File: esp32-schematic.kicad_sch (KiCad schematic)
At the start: 1 part, among them U1 ESP32-S3-DEVKITC-1U-N8R2

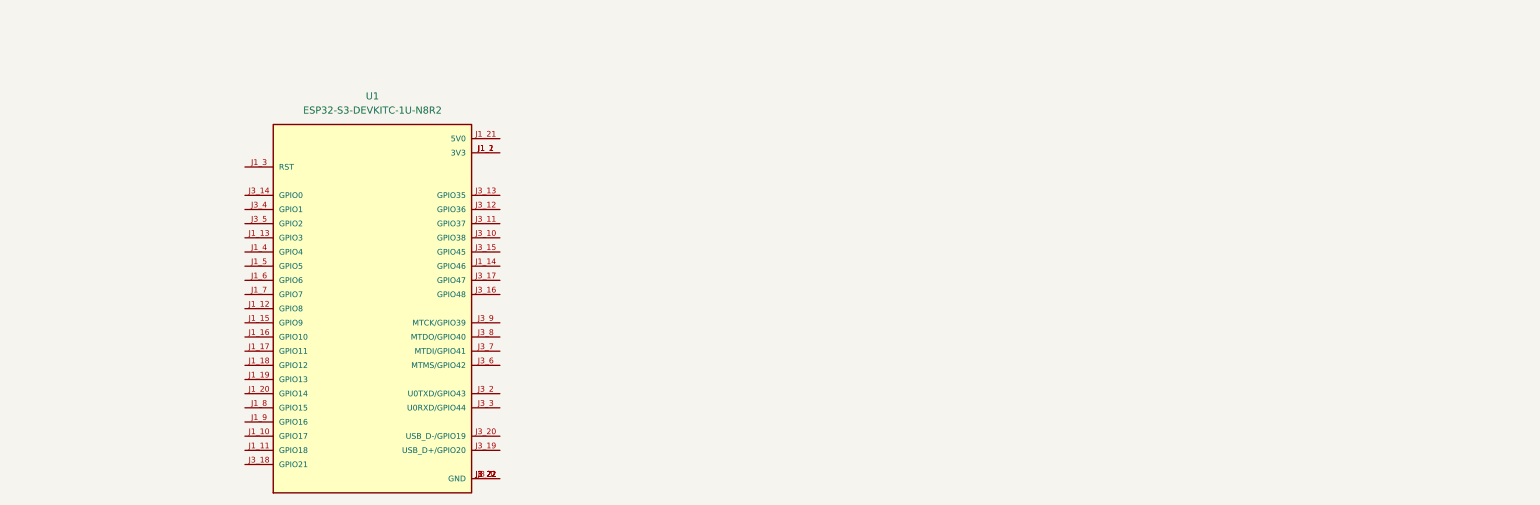
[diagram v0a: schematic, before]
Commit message: GPS added and CAN in progress
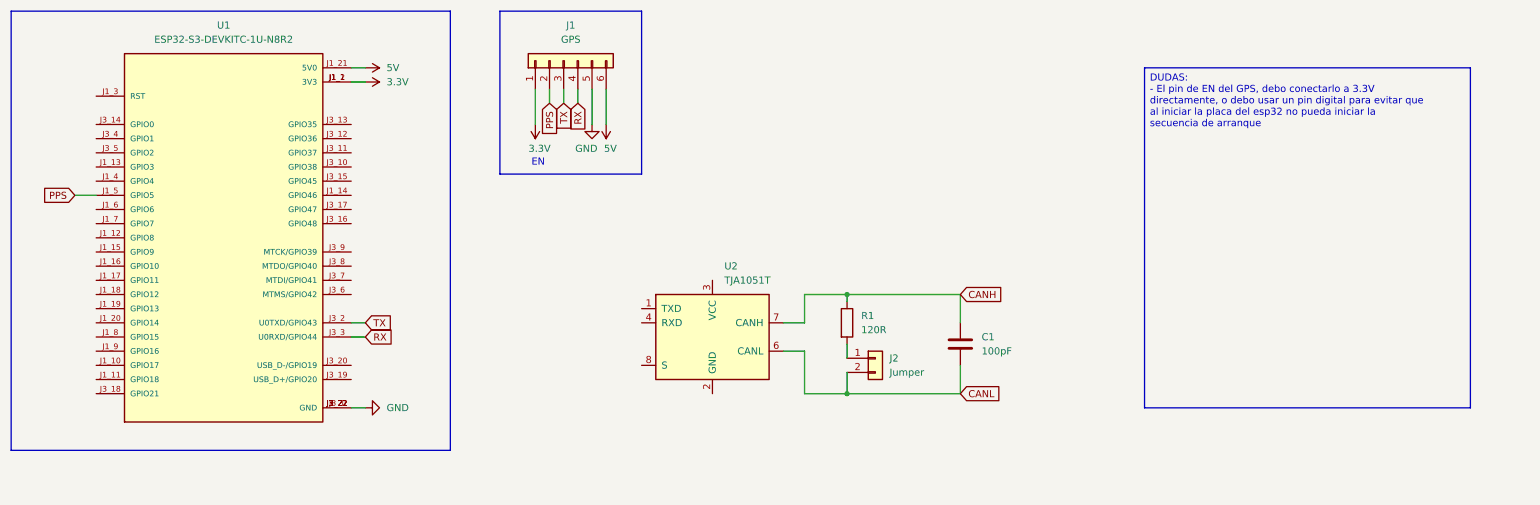
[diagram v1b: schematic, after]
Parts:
- added C1: 100pF, Capacitor_SMD:C_0805_2012Metric, symbol Device:C
- added J1: GPS, Conn_01x06:PinHeader_1x06_P2.54mm_Vertical, symbol Connector_Generic:Conn_01x06
- added J2: Jumper, Connector_PinHeader_1.00mm:PinHeader_1x02_P1.00mm_Vertical, symbol Connector_Generic:Conn_01x02
- added R1: 120R, Resistor_SMD:R_1206_3216Metric, symbol Device:R
- added U2: TJA1051T, Package_SO:SOIC-8_3.9x4.9mm_P1.27mm, symbol Interface_CAN_LIN:TJA1051T
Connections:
- net 3.3V: now reaches U1.J1_1 (3V3), U1.J1_2 (3V3)
- net 3.3V: now also J1.1 (Pin_1)
- net 5V: now reaches U1.J1_21 (5V0)
- net 5V: now also J1.6 (Pin_6)
- net GND: now reaches U1.J1_22 (GND), U1.J3_1 (GND), U1.J3_21 (GND), U1.J3_22 (GND)
- net GND: now also J1.5 (Pin_5)
- net PPS: now reaches U1.J1_5 (GPIO5)
- net PPS: now also J1.2 (Pin_2)
- net TX: now reaches U1.J3_2 (U0TXD/GPIO43)
- net TX: now also J1.3 (Pin_3)
- net RX: now reaches U1.J3_3 (U0RXD/GPIO44)
- net RX: now also J1.4 (Pin_4)
- new net: J2.1 (Pin_1), R1.2
- new net CANH: C1.1, R1.1, U2.7 (CANH)
- new net CANL: C1.2, J2.2 (Pin_2), U2.6 (CANL)
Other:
- note added: "EN"
- moved on the sheet: U1

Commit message: CAN in progress
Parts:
- added C2, C4: 0.1uF, Capacitor_SMD:C_0805_2012Metric, symbol Device:C
- added C3: 47uF, Capacitor_SMD:C_0805_2012Metric, symbol Device:C
- added R2: 120R, Resistor_SMD:R_1206_3216Metric, symbol Device:R
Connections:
- net 3.3V: now also U2.3 (VCC)
- net 5V: now also C2.1, C3.1
- net GND: now also U2.2 (GND), C2.2, C3.2, C4.2, R2.2
- net RX: now also U2.4 (RXD), C4.1
- net TX: now also U2.1 (TXD)
- net S: now reaches U2.8 (S)
- net S: now also R2.1
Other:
- note added: "CAN"
- note added: "ESP32"
- note added: "GPS"
- moved on the sheet: C1

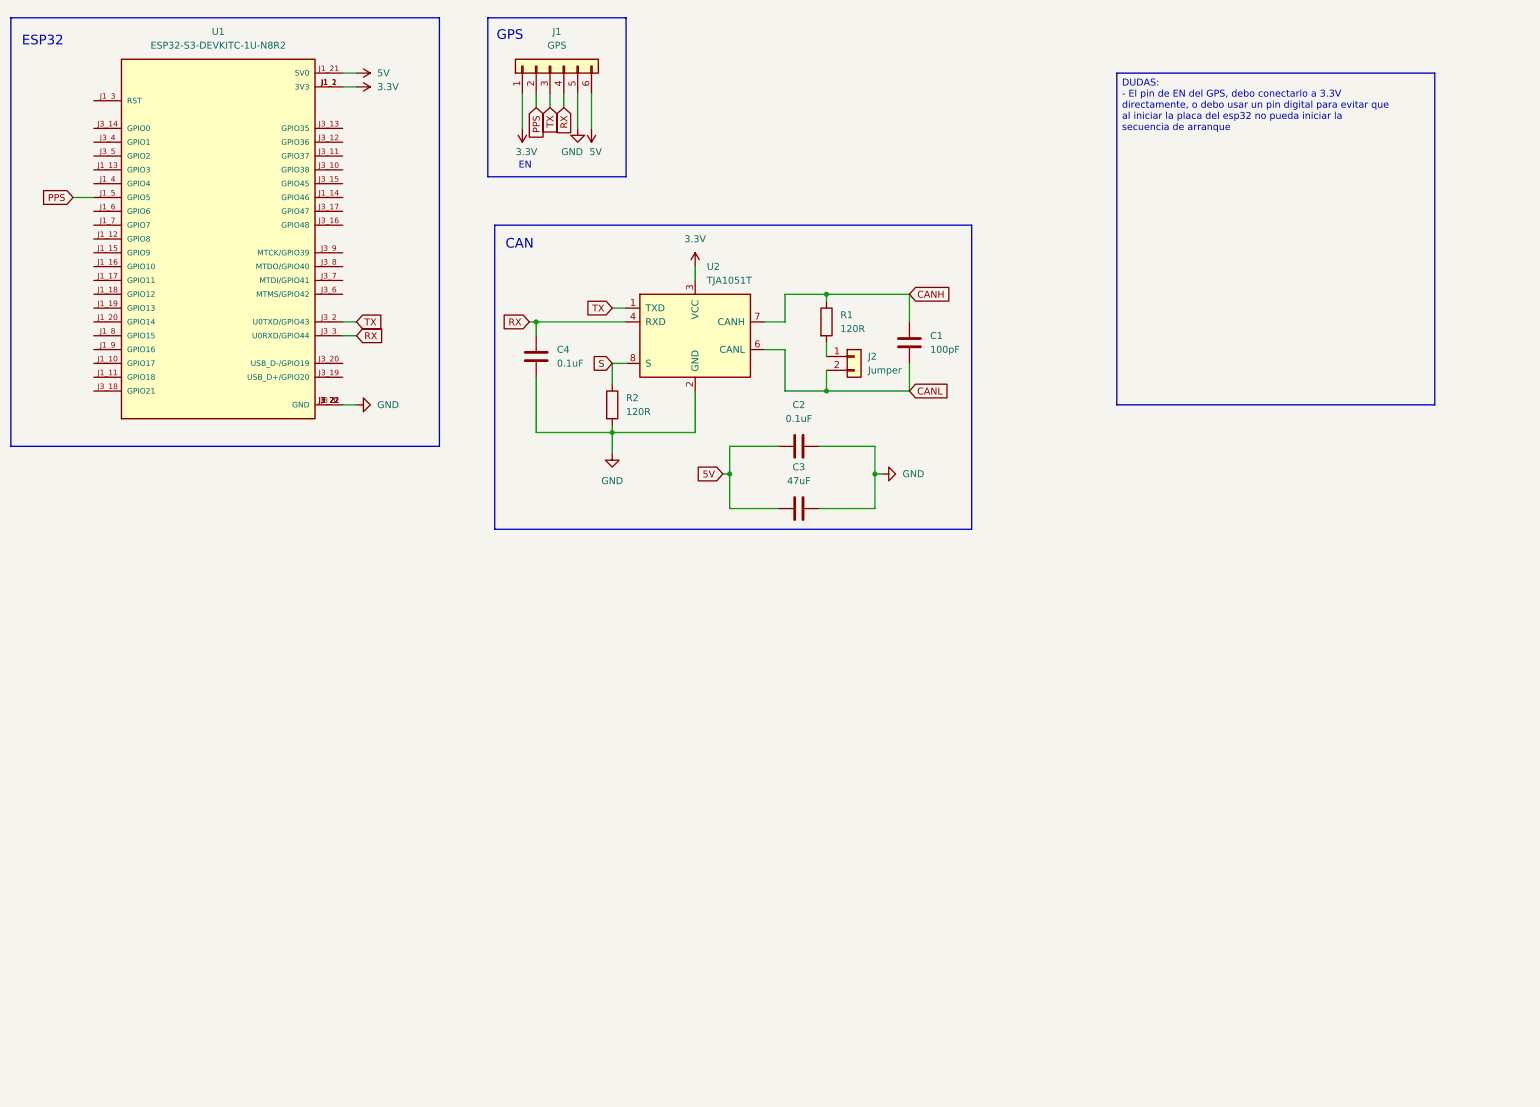
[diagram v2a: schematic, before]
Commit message: CAN schematic and IMU schematic ready
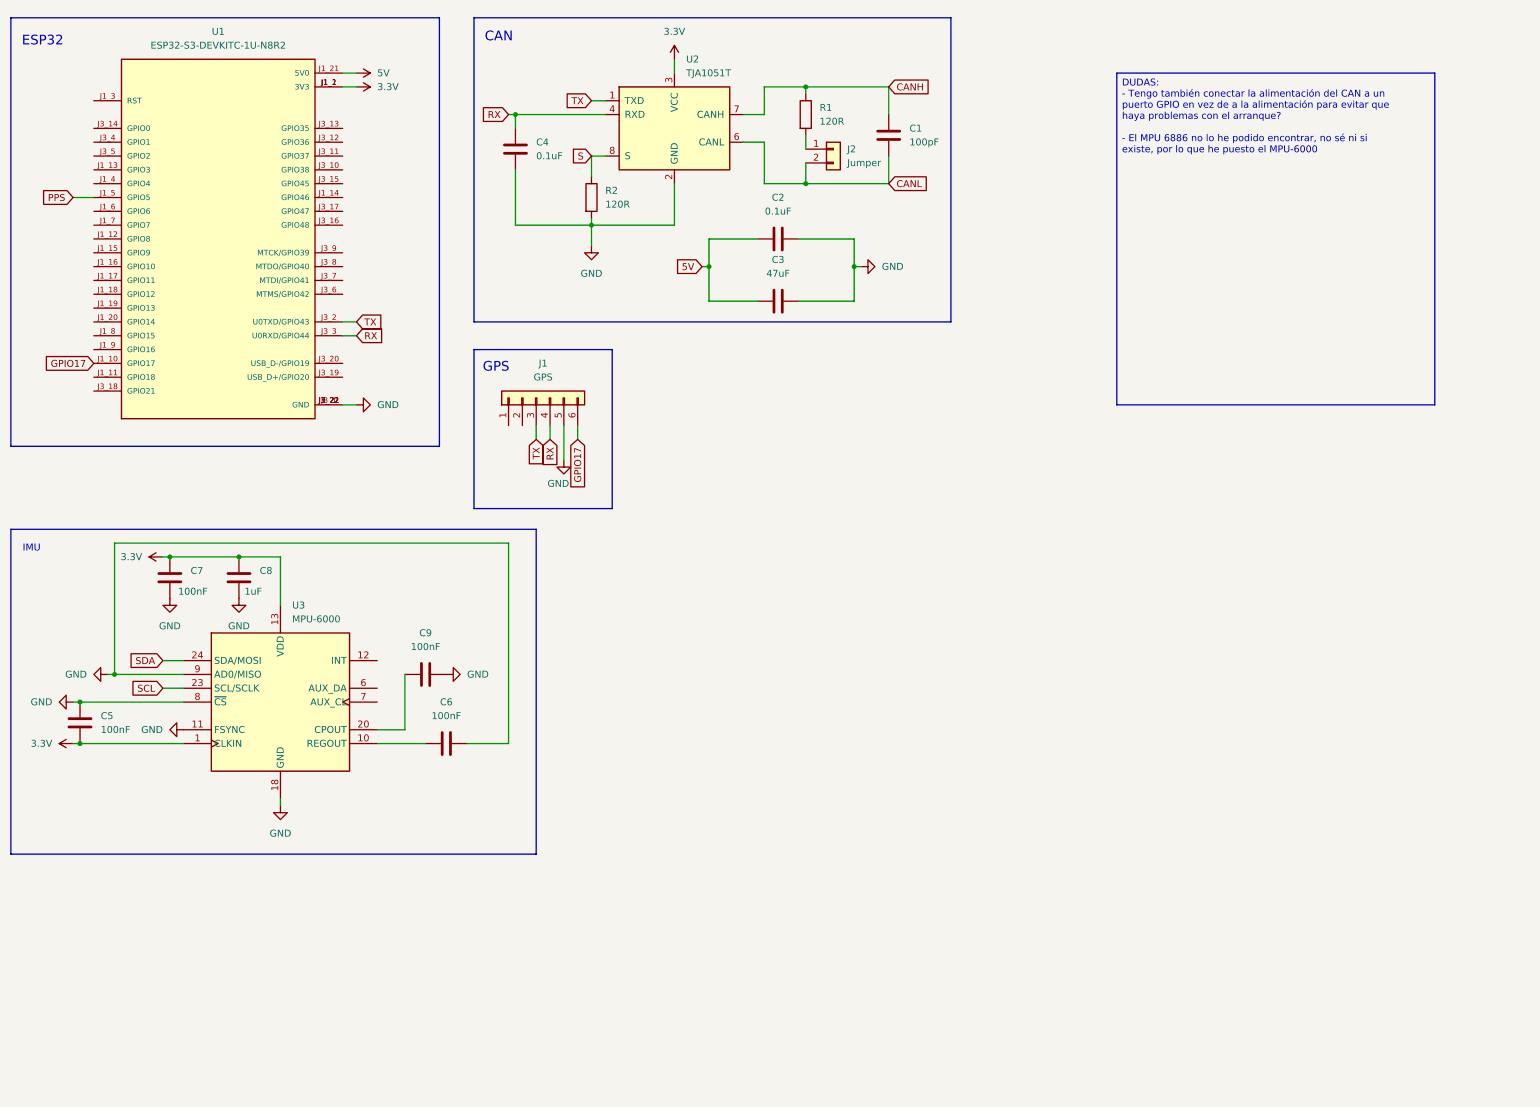
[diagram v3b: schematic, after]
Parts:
- added C5, C6, C7, C9: 100nF, Capacitor_SMD:C_0805_2012Metric, symbol Device:C
- added C8: 1uF, Capacitor_SMD:C_0805_2012Metric, symbol Device:C
- added U3: MPU-6000, Sensor_Motion:InvenSense_QFN-24_4x4mm_P0.5mm, symbol Sensor_Motion:MPU-6000
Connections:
- net 3.3V: now also C5.2, C7.1, C8.1, U3.1 (CLKIN), U3.13 (VDD); no longer J1.1 (Pin_1)
- net 5V: no longer J1.6 (Pin_6)
- net GND: now also C5.1, C6.2, C7.2, C8.2, C9.2, U3.11 (FSYNC), U3.18 (GND), U3.8 (~{CS}), U3.9 (AD0/MISO)
- net PPS: no longer J1.2 (Pin_2)
- net GPIO17: now reaches U1.J1_10 (GPIO17)
- net GPIO17: now also J1.6 (Pin_6)
- new net: C6.1, U3.10 (REGOUT)
- new net: C9.1, U3.20 (CPOUT)
- new net SCL: U3.23 (SCL/SCLK)
- new net SDA: U3.24 (SDA/MOSI)
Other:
- note added: "IMU"
- note removed: "EN"
- moved on the sheet: C1, C2, C3, C4, J1, J2, R1, R2, U2

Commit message: Readme Updated
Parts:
- J1: value GPS -> GN-2630G
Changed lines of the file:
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@@
 		)
 	)
-	(text_box "DUDAS:\n- Tengo también conectar la alimentación del CAN a un puerto GPIO en vez de a la alimentación para evitar que haya problemas con el arranque?\n\n- El MPU 6886 no lo he podido encontrar, no sé ni si existe, por lo que he puesto el MPU-6000"
+	(text_box "DUDAS:\n- Tengo también conectar la alimentación del CAN a un puerto GPIO en vez de a la alimentación para evitar que haya problemas con el arranque?\n\n- El MPU 6886 no lo he podido encontrar, no sé ni si existe como chip, por lo que he puesto el MPU-6000\n\n- Para el sensor de humedad no está disponible el chip QMP6988, por lo que no sé si hacer yo el chip o utilizar el sensor entero y atornillarlo a la placa o usar otro sensor diferente.\n"
 		(exclude_from_sim no)
 		(at 218.44 25.4 0)
@@
 			)
 		)
-		(property "Value" "GPS"
+		(property "Value" "GN-2630G"
 			(at 113.03 81.28 90)
 			(effects

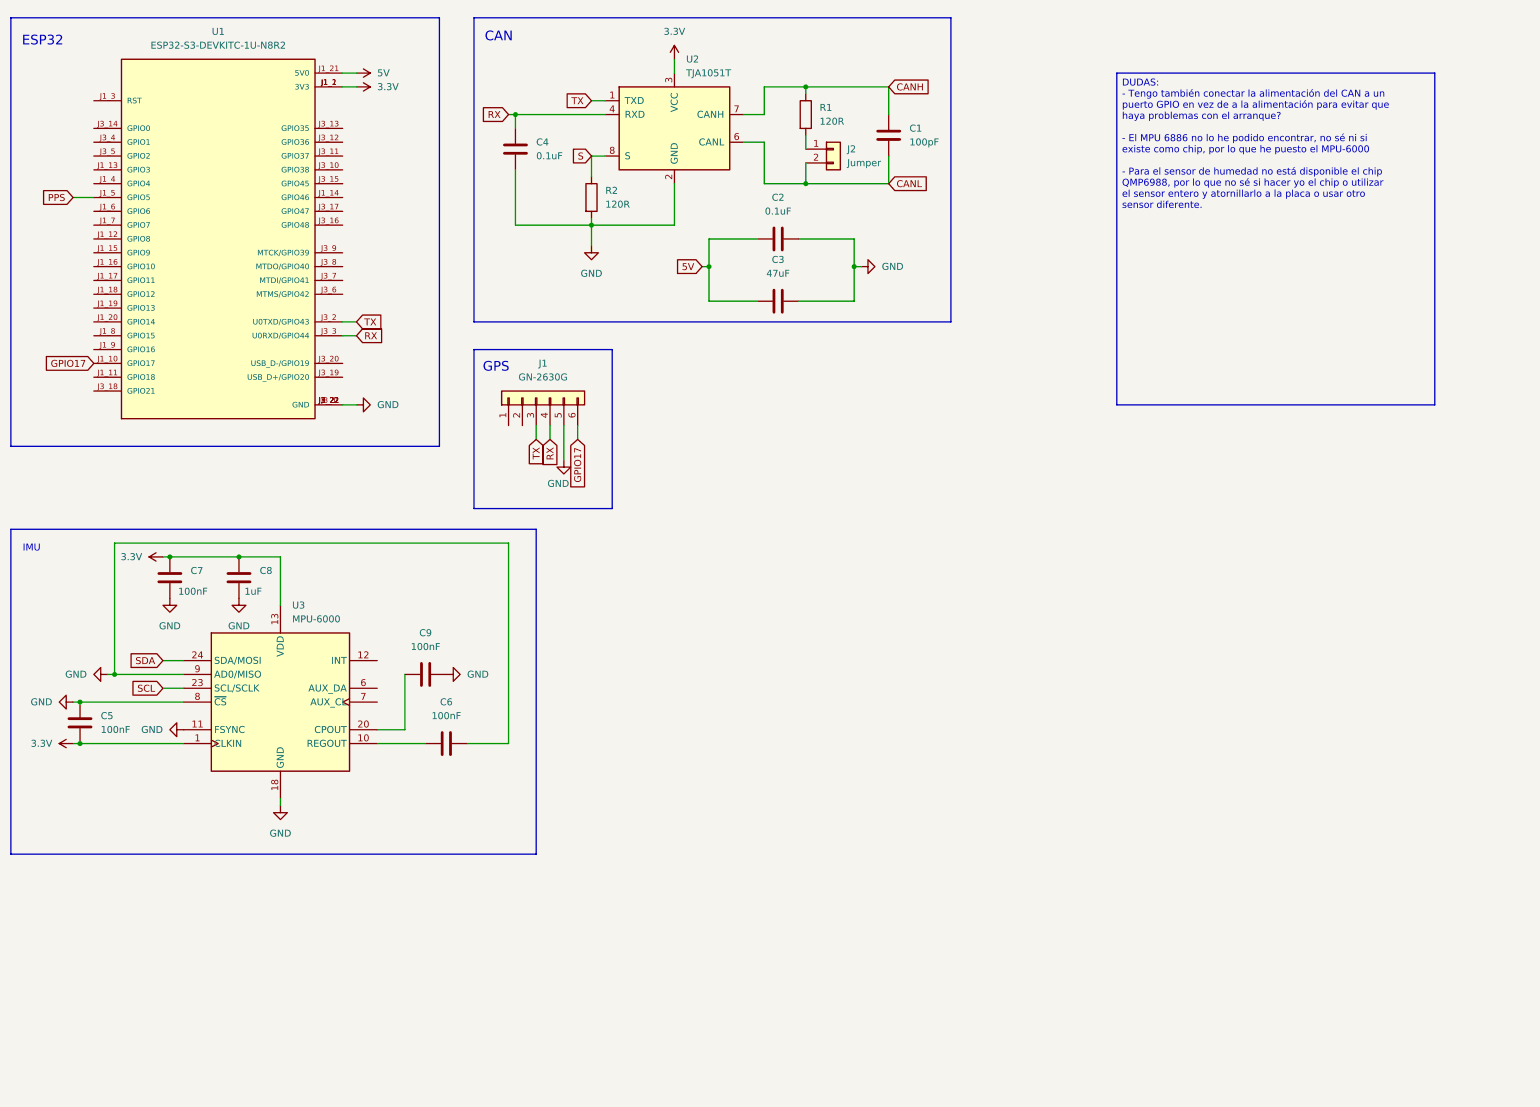
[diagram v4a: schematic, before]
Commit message: Micro SD added, IMU is now the MPU-9250, connections were moved in the ESP32 pins and the right footprints were added
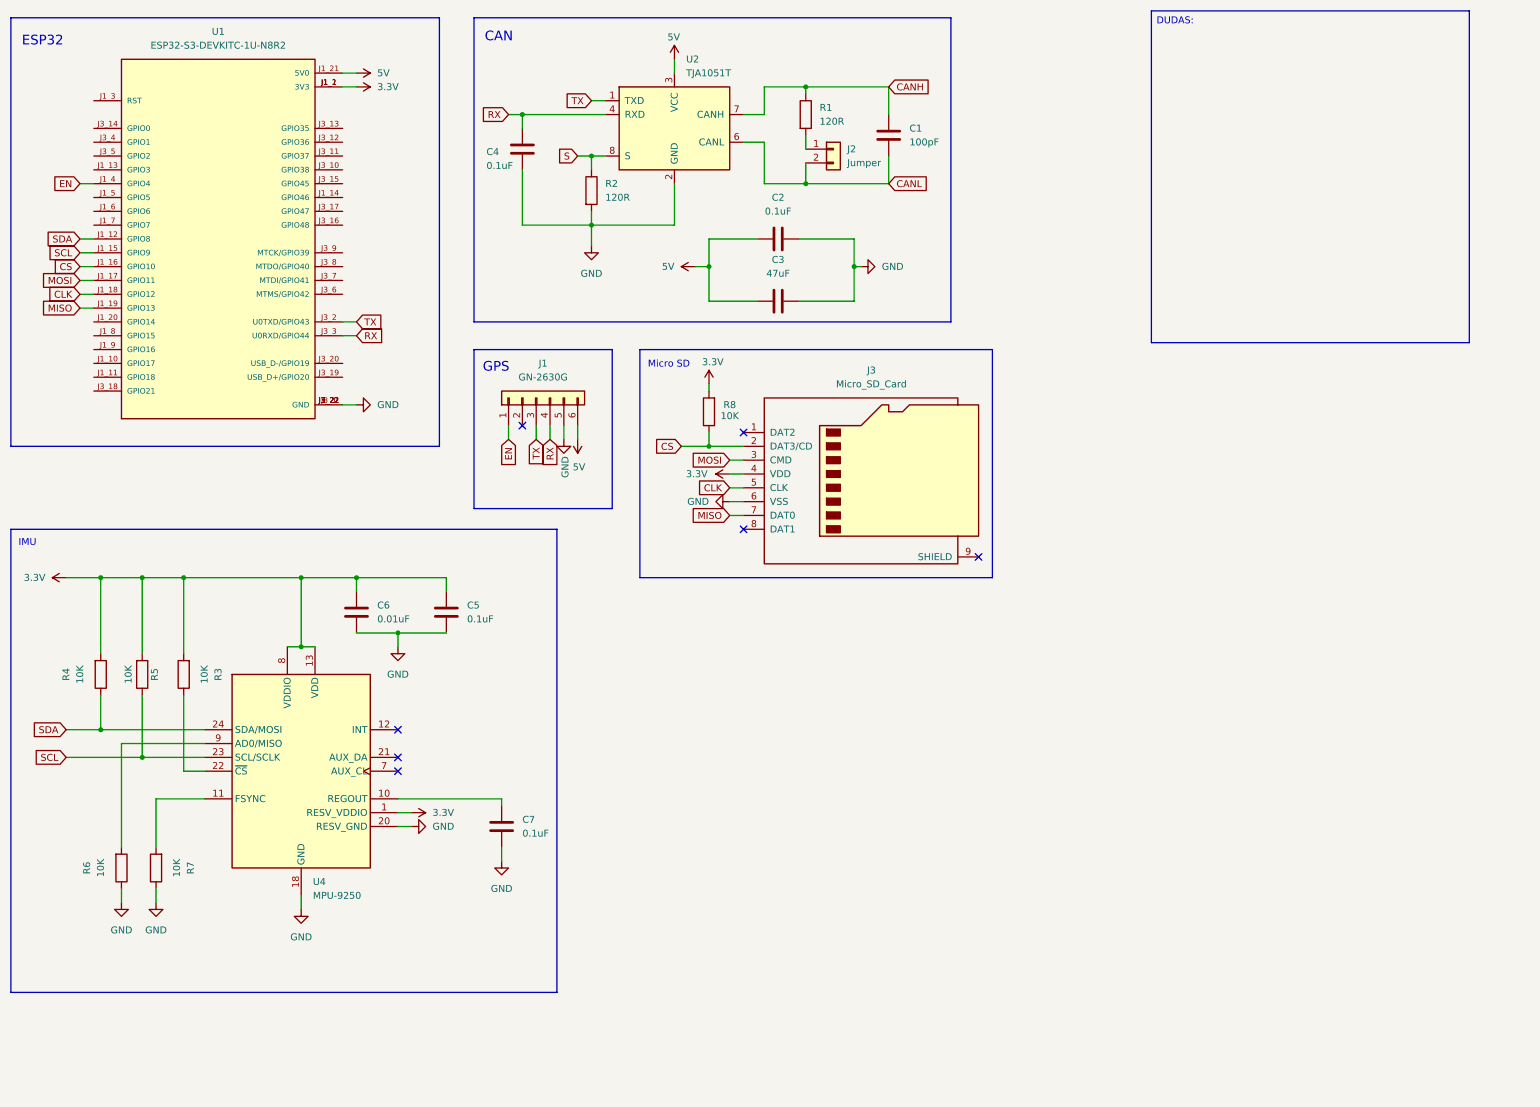
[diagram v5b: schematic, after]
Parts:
- removed C8: 1uF, Capacitor_SMD:C_0805_2012Metric, symbol Device:C
- removed C9: 100nF, Capacitor_SMD:C_0805_2012Metric, symbol Device:C
- removed U3: MPU-6000, Sensor_Motion:InvenSense_QFN-24_4x4mm_P0.5mm, symbol Sensor_Motion:MPU-6000
- added J3: Micro_SD_Card, Connector_Card:microSD_HC_Molex_104031-0811, symbol Connector:Micro_SD_Card
- added R3, R4, R5, R6, R7, R8: 10K, Resistor_SMD:R_1206_3216Metric, symbol Device:R
- added U4: MPU-9250, Sensor_Motion:InvenSense_QFN-24_3x3mm_P0.4mm, symbol Sensor_Motion:MPU-9250
- C5, C7: value 100nF -> 0.1uF
- C6: value 100nF -> 0.01uF
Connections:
- net 3.3V: now also C5.1, C6.1, J3.4 (VDD), R3.2, R4.2, R5.2, R8.2, U4.1 (RESV_VDDIO), U4.13 (VDD), U4.8 (VDDIO); no longer C5.2, C7.1, U2.3 (VCC)
- net 5V: now also J1.6 (Pin_6), U2.3 (VCC)
- net GND: now also C5.2, J3.6 (VSS), R6.1, R7.1, U4.18 (GND), U4.20 (RESV_GND); no longer C5.1
- net SCL: now also U1.J1_15 (GPIO9), R5.1, U4.23 (SCL/SCLK)
- net SDA: now also U1.J1_12 (GPIO8), R4.1, U4.24 (SDA/MOSI)
- net EN: now reaches J1.1 (Pin_1)
- net EN: now also U1.J1_4 (GPIO4)
- net CS: now reaches U1.J1_16 (GPIO10)
- net CS: now also J3.2 (DAT3/CD), R8.1
- net MOSI: now reaches U1.J1_17 (GPIO11)
- net MOSI: now also J3.3 (CMD)
- net CLK: now reaches U1.J1_18 (GPIO12)
- net CLK: now also J3.5 (CLK)
- net MISO: now reaches U1.J1_19 (GPIO13)
- net MISO: now also J3.7 (DAT0)
- net GPIO17: no longer names the net of U1.J1_10 (GPIO17)
- net GPIO17: no longer J1.6 (Pin_6)
- net PPS: no longer names the net of U1.J1_5 (GPIO5)
- new net: R3.1, U4.22 (~{CS})
- new net: R7.2, U4.11 (FSYNC)
- new net: C7.1, U4.10 (REGOUT)
- new net: R6.2, U4.9 (AD0/MISO)
- no-connect marks 0 -> 7
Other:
- note added: "Micro SD"
- moved on the sheet: C4, R2
